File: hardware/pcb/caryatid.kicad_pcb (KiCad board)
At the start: 2 copper layers, 150 x 90 mm, 135 parts, among them J1 DC in, J10 FSR, J11 Digital bus, J12 RGB status, J13 Comms A - Qwiic, J14 Mic bias return, J15 Comms B - module, J16 Expansion / SPI1, J17 Audio out L/R/G, J18 Audio in L/R/rtn, J19 Comms A - module, J3 Latch switch, J4 Charge LEDs, J5 Analogue bus, J6 SW1 switch, J7 SW2 switch, J8 SW3 switch, J9 Soft pot, U1 BQ24074RGT, U2 TPS61023DRL, U3 74HC14, U4 MCP6002

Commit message: Silkscreen the capsule selector table; bring the docs to the jumpers
ADR 0009 accepts one real cost of jumpers over three sockets: a jumper
is mis-settable where plugging into the right hole is not. The
mitigation is that the board carries its own procedure, so the table
prints the IDENTIFICATION TEST alongside the positions:

  MIC CAPSULE            MEASURE DC OHMS
       JP1 JP2 JP3       OPEN     = ELEC
  ELEC  12  12  12       150-600R = DYN
  DYN   --  12  23       50-300R  = CARB
  CARB  23  23  --       UNSTABLE = CARB

Read the meter, read the row, set three shunts. A legend naming only the
positions would still have sent you to the datasheet.

"12" and "23" are pin PAIRS, not positions -- pin 1 is marked on the
silkscreen while "top" depends on which way the board is held.

13.2 x 12.0 mm at 0.8 mm text, placed by tools/jumper_legend.py against
pin_labels obstacle model and locked.

TWO DEFECTS CAUGHT BY DRC, BOTH MINE:

  A 0.7 mm fallback size. It fit, and it is UNDER JLCs 0.8 mm silk
  floor -- an illegible legend is not a mitigation. There is now no
  fallback; the search widened to a 1 mm polar grid instead.

  Line pitch of 1.25x text produced NINE silk_overlap violations where
  the lines clashed with EACH OTHER, 0.08 mm against 0.25 required.
  Text that is legal individually still has to clear the line above it.
  Pitch is now derived from pin_labels.th_split -- ink height plus the
  silk rule -- rather than chosen.

DOCS: audio.md, integration.md and values.md described the input as DNP
and solder-selected. audio.md now leads with the jumper tables and keeps
the old design as a note explaining why it changed; integration.md
carries the capsule table and the warning that JLC does not fit shunts;
values.md marks R52 as drawing current only on the carbon setting and
adds R51 at 1.5 mA. Part counts corrected: 110 placed, 17 DNP, BT1
self-fit.

Also records why R59/R60/R61 are populated -- U4 is a dual, and section
B would otherwise sit with floating 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
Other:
- board text added: "150-600R = DYN"
- board text added: "50-300R = CARB"
- board text added: "CARB 23 23 --"
- board text added: "DYN -- 12 23"
- board text added: "ELEC 12 12 12"
- board text added: "JP1 JP2 JP3"
- board text added: "MEASURE DC OHMS"
- board text added: "MIC CAPSULE"
- board text added: "OPEN = ELEC"
- board text added: "UNSTABLE = CARB"
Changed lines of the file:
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@@
 		(layer "Edge.Cuts")
+	)
+	(gr_text "MIC CAPSULE"
+		(locked yes)
+		(at 127.5465 94.6768)
+		(layer "F.SilkS")
+		(effects
+			(font
+				(size 0.8 0.8)
+				(thickness 0.15)
+			)
+			(justify left)
+		)
+	)
+	(gr_text "     JP1 JP2 JP3"
+		(locked yes)
+		(at 127.5465 95.8768)
+		(layer "F.SilkS")
+		(effects
+			(font
+				(size 0.8 0.8)
+				(thickness 0.15)
+			)
+			(justify left)
+		)
+	)
+	(gr_text "ELEC  12  12  12"
+		(locked yes)
+		(at 127.5465 97.0768)
+		(layer "F.SilkS")
+		(effects
+			(font
+				(size 0.8 0.8)
+				(thickness 0.15)
+			)
+			(justify left)
+		)
+	)
+	(gr_text "DYN   --  12  23"
+		(locked yes)
+		(at 127.5465 98.2768)
+		(layer "F.SilkS")
+		(effects
+			(font
+				(size 0.8 0.8)
+				(thickness 0.15)
+			)
+			(justify left)
+		)
+	)
+	(gr_text "CARB  23  23  --"
+		(locked yes)
+		(at 127.5465 99.4768)
+		(layer "F.SilkS")
+		(effects
+			(font
+				(size 0.8 0.8)
+				(thickness 0.15)
+			)
+			(justify left)
+		)
+	)
+	(gr_text "MEASURE DC OHMS"
+		(locked yes)
+		(at 127.5465 100.6768)
+		(layer "F.SilkS")
+		(effects
+			(font
+				(size 0.8 0.8)
+				(thickness 0.15)
+			)
+			(justify left)
+		)
+	)
+	(gr_text "OPEN     = ELEC"
+		(locked yes)
+		(at 127.5465 101.8768)
+		(layer "F.SilkS")
+		(effects
+			(font
+				(size 0.8 0.8)
+				(thickness 0.15)
+			)
+			(justify left)
+		)
+	)
+	(gr_text "150-600R = DYN"
+		(locked yes)
+		(at 127.5465 103.0768)
+		(layer "F.SilkS")
+		(effects
+			(font
+				(size 0.8 0.8)
+				(thickness 0.15)
+			)
+			(justify left)
+		)
+	)
+	(gr_text "50-300R  = CARB"
+		(locked yes)
+		(at 127.5465 104.2768)
+		(layer "F.SilkS")
+		(effects
+			(font
+				(size 0.8 0.8)
+				(thickness 0.15)
+			)
+			(justify left)
+		)
+	)
+	(gr_text "UNSTABLE = CARB"
+		(locked yes)
+		(at 127.5465 105.4768)
+		(layer "F.SilkS")
+		(effects
+			(font
+				(size 0.8 0.8)
+				(thickness 0.15)
+			)
+			(justify left)
+		)
 	)
 	(gr_line

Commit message: Add per-position labels at each jumper: the position is the answer
A table tells you which combination to use. It does not tell you what
the shunt in your fingers is about to do. These do:

       ELE    AMP    101      <- top pair, pins 1-2
       JP1    JP2    JP3
       CAR    BYP    256      <- bottom pair, pins 2-3

Above the header means fit the shunt on the top pair, below means the
bottom pair, because the jumpers stand vertically with pin 1 uppermost.
No shunt on JP1 at all is dynamic. Three characters each -- the headers
are 4.59 mm apart and anything longer collides with its neighbour.

The capsule table stays: it carries the combinations and the DC-ohms
identification test, which is what makes the legend a procedure. The
position labels remove the cross-reference while you are holding
tweezers.

A drawn pictogram grid was considered and rejected on space. The largest
clear block anywhere near the jumpers is 13 x 12 mm -- 16 x 14 exists
but 39 mm away, too far to be useful -- and drawn cells would have
displaced the ohms key, which is the part worth keeping.

ONE DEFECT, CAUGHT BY THE TOOL RATHER THAN BY DRC: the first run placed
only three of six labels and said so. The reference designators sit
2.38 mm above pin 1, so a top label has to clear them and land ABOVE the
reference, around 4 mm out; the gap search stopped at 3.5. It reported
the miss instead of forcing a placement, which is the behaviour worth
having -- a silently half-drawn legend is worse than none.
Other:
- board text added: "101"
- board text added: "256"
- board text added: "AMP"
- board text added: "BYP"
- board text added: "CAR"
- board text added: "ELE"
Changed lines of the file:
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@@
+		)
+	)
+	(gr_text "ELE"
+		(locked yes)
+		(at 142.5450 95.1700)
+		(layer "F.SilkS")
+		(effects
+			(font
+				(size 0.8 0.8)
+				(thickness 0.15)
+			)
+		)
+	)
+	(gr_text "CAR"
+		(locked yes)
+		(at 142.5450 106.8500)
+		(layer "F.SilkS")
+		(effects
+			(font
+				(size 0.8 0.8)
+				(thickness 0.15)
+			)
+		)
+	)
+	(gr_text "AMP"
+		(locked yes)
+		(at 147.1350 95.1700)
+		(layer "F.SilkS")
+		(effects
+			(font
+				(size 0.8 0.8)
+				(thickness 0.15)
+			)
+		)
+	)
+	(gr_text "BYP"
+		(locked yes)
+		(at 147.1350 106.8500)
+		(layer "F.SilkS")
+		(effects
+			(font
+				(size 0.8 0.8)
+				(thickness 0.15)
+			)
+		)
+	)
+	(gr_text "101"
+		(locked yes)
+		(at 151.7250 95.1700)
+		(layer "F.SilkS")
+		(effects
+			(font
+				(size 0.8 0.8)
+				(thickness 0.15)
+			)
+		)
+	)
+	(gr_text "256"
+		(locked yes)
+		(at 151.7250 106.8500)
+		(layer "F.SilkS")
+		(effects
+			(font
+				(size 0.8 0.8)
+				(thickness 0.15)
+			)
 		)
 	)

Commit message: Strip the front text table; the artwork replaces it
Removed the 10-line capsule table from F.SilkS, freeing 13.2 x 12 mm
near the jumpers at about (134, 103). Matt is placing the SVG himself.

KEPT: the six per-position labels at the headers -- ELE/CAR, AMP/BYP,
101/256. They are not the same thing as the table. The table explains
which combination a capsule wants and can live anywhere, including the
back or a printed sheet; the position labels sit ON the jumpers and say
what the shunt in your fingers is about to do. Nothing else can do that
job, and they cost 6 x 3 characters.

Say so if they should go too -- tools/jumper_legend.py --strip --apply
removes both, --strip-table removes only the table.

MEASURED WHILE LOOKING AT THIS, and worth recording because it decides
where the artwork can go:

  front, largest clear area anywhere   26 x 23.4 mm  (scale 0.049)
  back, clearing all 132 THT pads      45.2 x 40.7 mm (scale 0.0850)

The 0.085 scale is right and it does not fit on the front at any
position -- at 0.049 the smallest outlined text lands at 0.54 mm, well
under JLC 0.8 mm silk floor, so it would print as mush. On the back it
fits centred at (121.6, 52.35) with the whole face otherwise empty:
zero B.SilkS objects and zero back-side footprints.

Board still clean: eleven of eleven, no silk_overlap, 110 of 110 sourced,
fab package rebuilt.
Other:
- board text removed: "150-600R = DYN"
- board text removed: "50-300R = CARB"
- board text removed: "CARB 23 23 --"
- board text removed: "DYN -- 12 23"
- board text removed: "ELEC 12 12 12"
- board text removed: "JP1 JP2 JP3"
- board text removed: "MEASURE DC OHMS"
- board text removed: "MIC CAPSULE"
- board text removed: "OPEN = ELEC"
- board text removed: "UNSTABLE = CARB"
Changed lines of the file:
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@@
 		(layer "Edge.Cuts")
-	)
-	(gr_text "MIC CAPSULE"
-		(locked yes)
-		(at 127.5465 94.6768)
-		(layer "F.SilkS")
-		(effects
-			(font
-				(size 0.8 0.8)
-				(thickness 0.15)
-			)
-			(justify left)
-		)
-	)
-	(gr_text "     JP1 JP2 JP3"
-		(locked yes)
-		(at 127.5465 95.8768)
-		(layer "F.SilkS")
-		(effects
-			(font
-				(size 0.8 0.8)
-				(thickness 0.15)
-			)
-			(justify left)
-		)
-	)
-	(gr_text "ELEC  12  12  12"
-		(locked yes)
-		(at 127.5465 97.0768)
-		(layer "F.SilkS")
-		(effects
-			(font
-				(size 0.8 0.8)
-				(thickness 0.15)
-			)
-			(justify left)
-		)
-	)
-	(gr_text "DYN   --  12  23"
-		(locked yes)
-		(at 127.5465 98.2768)
-		(layer "F.SilkS")
-		(effects
-			(font
-				(size 0.8 0.8)
-				(thickness 0.15)
-			)
-			(justify left)
-		)
-	)
-	(gr_text "CARB  23  23  --"
-		(locked yes)
-		(at 127.5465 99.4768)
-		(layer "F.SilkS")
-		(effects
-			(font
-				(size 0.8 0.8)
-				(thickness 0.15)
-			)
-			(justify left)
-		)
-	)
-	(gr_text "MEASURE DC OHMS"
-		(locked yes)
-		(at 127.5465 100.6768)
-		(layer "F.SilkS")
-		(effects
-			(font
-				(size 0.8 0.8)
-				(thickness 0.15)
-			)
-			(justify left)
-		)
-	)
-	(gr_text "OPEN     = ELEC"
-		(locked yes)
-		(at 127.5465 101.8768)
-		(layer "F.SilkS")
-		(effects
-			(font
-				(size 0.8 0.8)
-				(thickness 0.15)
-			)
-			(justify left)
-		)
-	)
-	(gr_text "150-600R = DYN"
-		(locked yes)
-		(at 127.5465 103.0768)
-		(layer "F.SilkS")
-		(effects
-			(font
-				(size 0.8 0.8)
-				(thickness 0.15)
-			)
-			(justify left)
-		)
-	)
-	(gr_text "50-300R  = CARB"
-		(locked yes)
-		(at 127.5465 104.2768)
-		(layer "F.SilkS")
-		(effects
-			(font
-				(size 0.8 0.8)
-				(thickness 0.15)
-			)
-			(justify left)
-		)
-	)
-	(gr_text "UNSTABLE = CARB"
-		(locked yes)
-		(at 127.5465 105.4768)
-		(layer "F.SilkS")
-		(effects
-			(font
-				(size 0.8 0.8)
-				(thickness 0.15)
-			)
-			(justify left)
-		)
 	)
 	(gr_text "ELE"

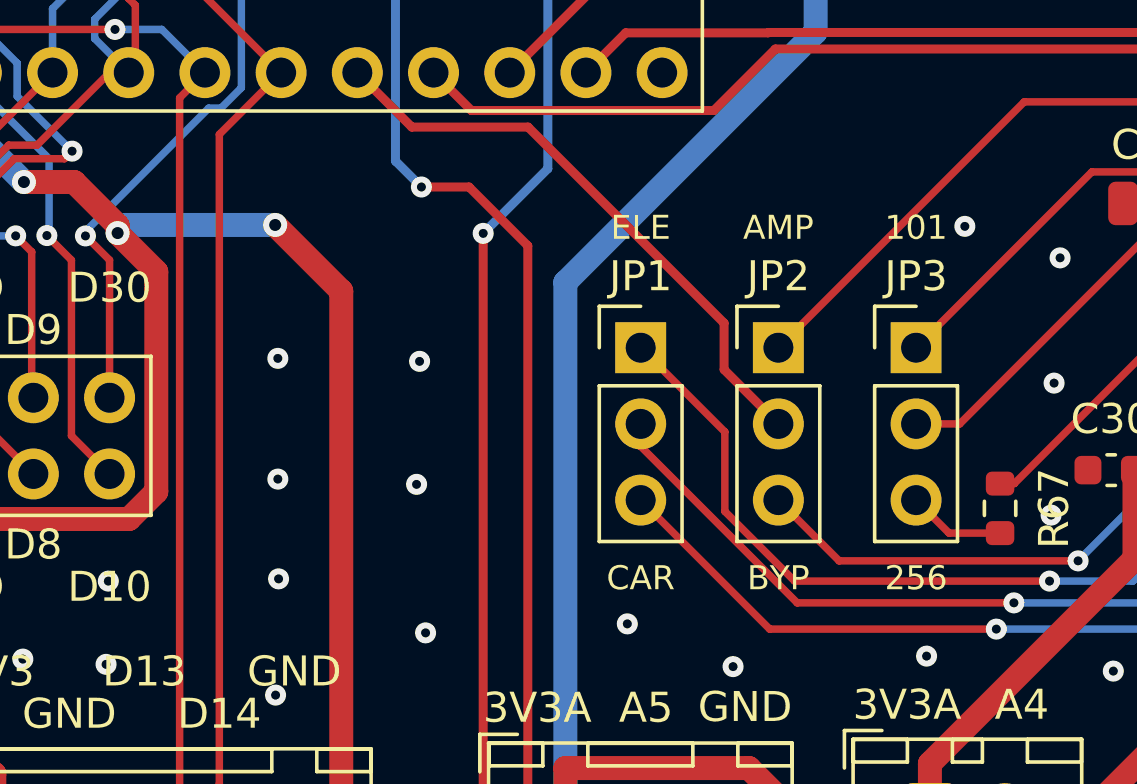
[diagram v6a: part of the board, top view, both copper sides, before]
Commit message: Mic capsule legend: pictogram artwork, headers at the 0.8 mm floor
The front legend is now Matt drawn pictogram -- a filled bar over the
shunted pair, open dots elsewhere, one row per capsule -- with native
KiCad text for the row and column labels. It replaces the text table,
which was accurate and not clear.

Headers dropped 1.0 -> 0.8 mm: Elect, Dyn, Carb, JP1/bias, JP2/path,
JP3/gain. 0.8 mm is JLC text-height floor exactly, and it is what seven
pin labels on this board already use, so it is a proven-fabricable
precedent rather than a spec reading. Thickness stays 0.15, the line
floor. GND and D13 left at 1.0 -- they belong to J16 and J15, not the
legend. The reduction also separated "bias" and "path", which had been
reading as one word.

Also nudged the Elect label 0.20 mm left; it sat 0.154 mm from the
artwork against a 0.25 mm rule.

TWO OF MY OWN CHECKS WERE WRONG HERE AND BOTH ARE WORTH RECORDING:

I called an earlier version of the artwork a failure by demanding that
90% of SHAPES clear 0.8 mm. That conflates two different rules -- 0.8 mm
is the minimum TEXT HEIGHT, for characters that must be legible, while
0.15 mm is the minimum FEATURE WIDTH that applies to drawn artwork. The
redrawn version clears the real floor by 3.2x (thinnest feature
0.476 mm, nothing under 0.15). It passed; the test did not.

The first version genuinely did fail -- 149 of 221 shapes under 0.15 mm,
60 of them literally zero area -- because outlined text at 0.0188 scale
collapses. That finding stands. What changed is that the redraw uses
dots and bars plus native text, so there is no outlined lettering left
to collapse.

And a gap calculation predicted "bias"/"path" overlapping by 0.64 mm,
which DRC does not see. tw() was not measuring what I assumed for
multi-line centred text. DRC and the render are the authorities.

Board: eleven of eleven, no silk_overlap, 0 unconnected, 110 of 110
sourced, fab package rebuilt.
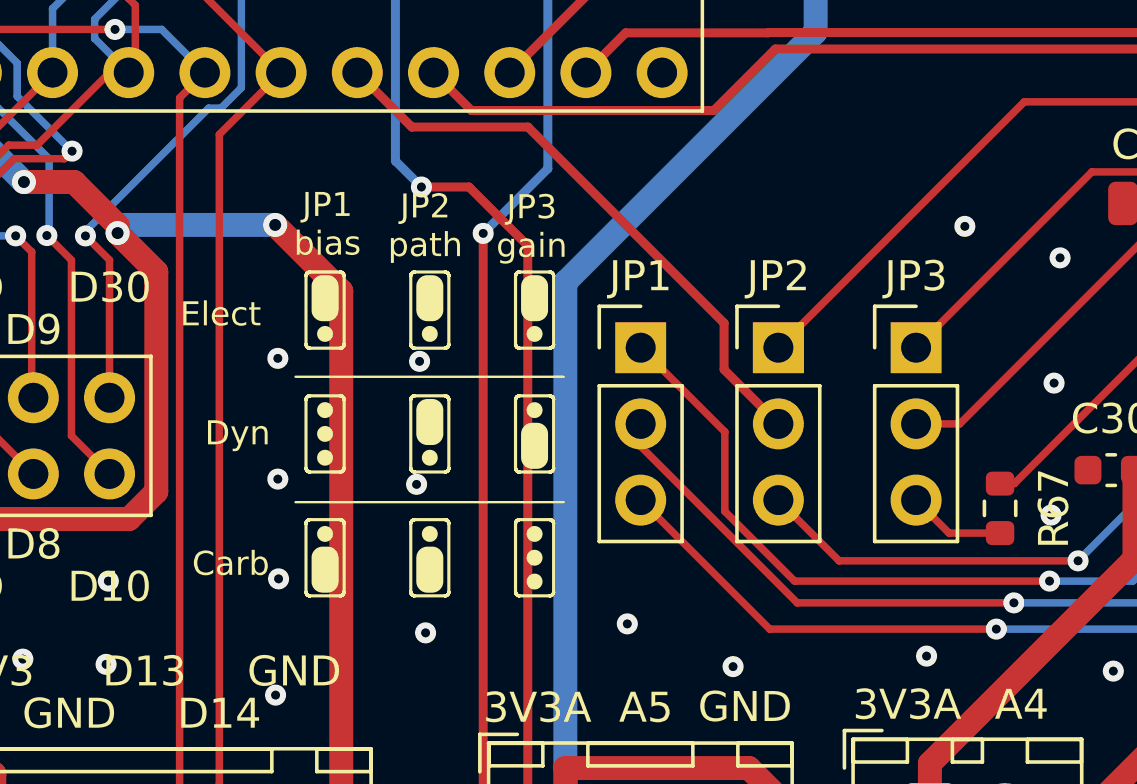
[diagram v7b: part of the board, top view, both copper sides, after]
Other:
- board text added: "Carb"
- board text added: "Dyn"
- board text added: "Elect"
- board text added: "JP1 bias"
- board text added: "JP2 path"
- board text added: "JP3 gain"
- board text removed: "101"
- board text removed: "256"
- board text removed: "AMP"
- board text removed: "BYP"
- board text removed: "CAR"
- board text removed: "ELE"
